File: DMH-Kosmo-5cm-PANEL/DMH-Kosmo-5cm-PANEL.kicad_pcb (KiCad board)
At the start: 2 copper layers, 50 x 200 mm, 4 parts

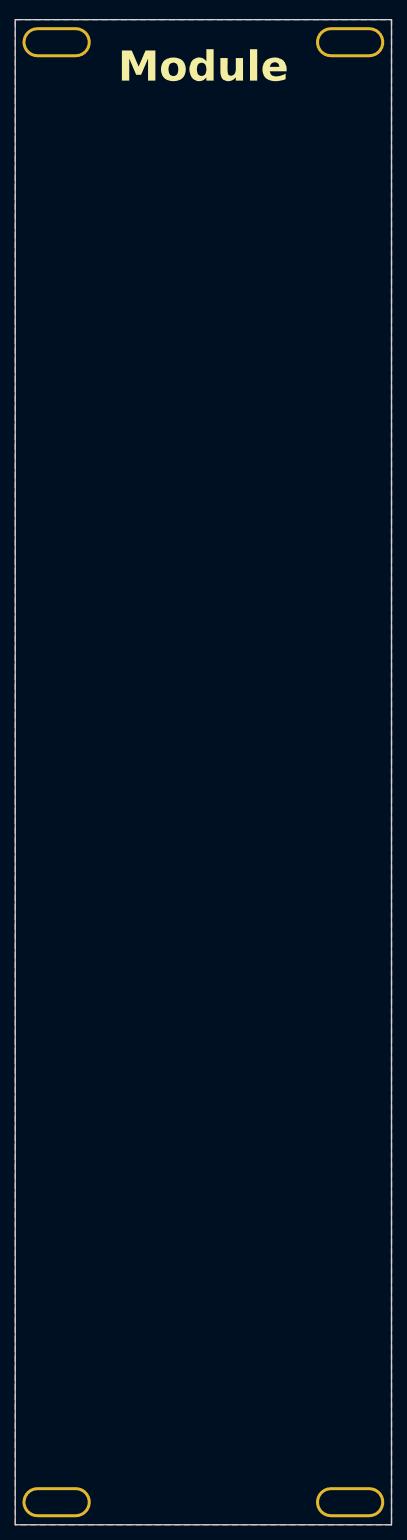
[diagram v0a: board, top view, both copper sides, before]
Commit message: Finished 5cm Panel template
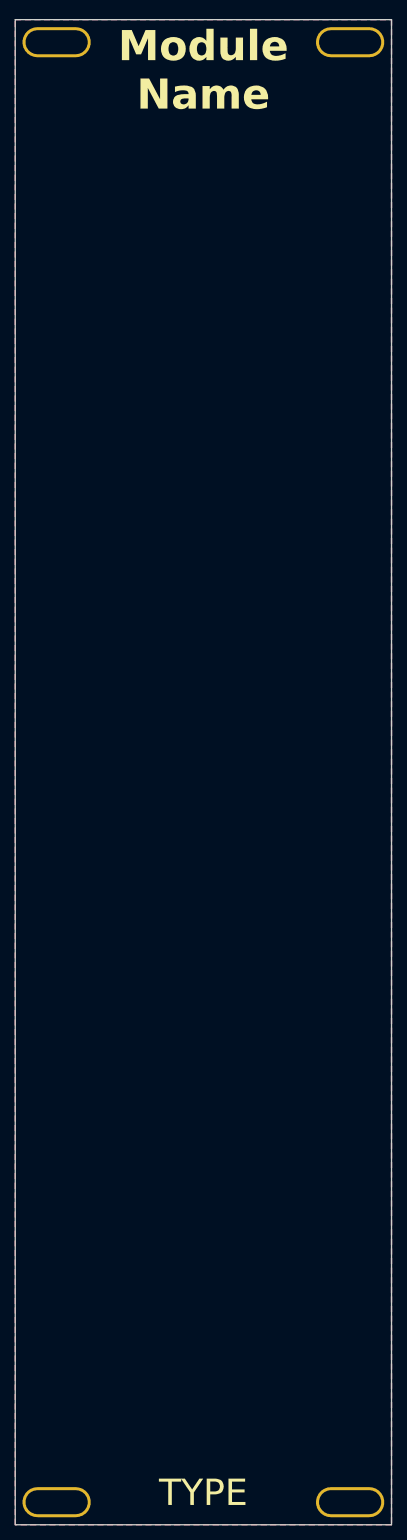
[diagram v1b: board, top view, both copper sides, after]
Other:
- board text added: "Module Name"
- board text added: "TYPE"
- board text removed: "Module"

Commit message: Updated 5cm and 10 templates
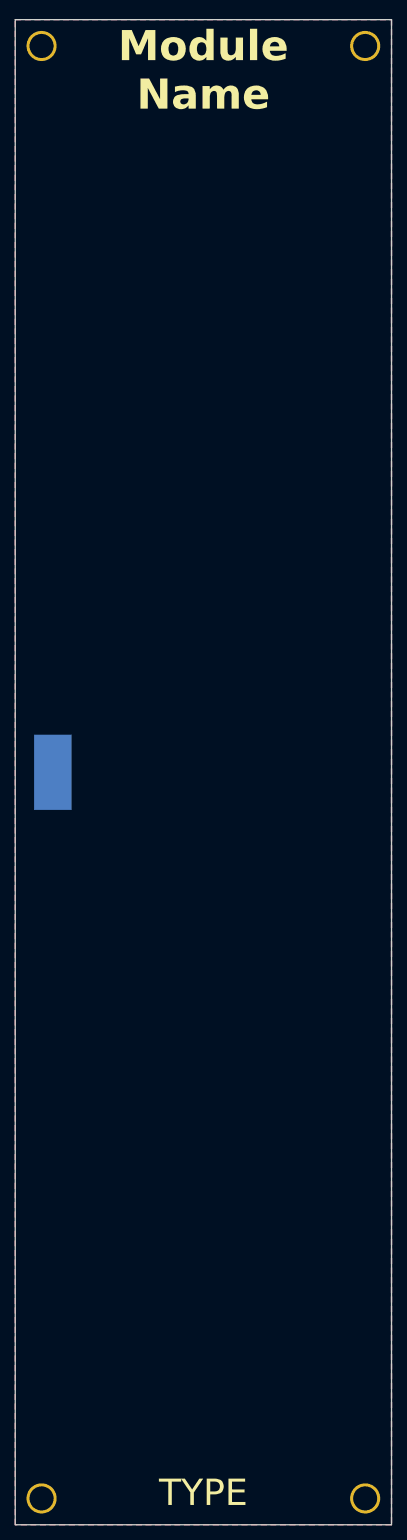
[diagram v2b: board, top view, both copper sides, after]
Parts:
- added J0: Panel_GND_Solder_Wire_Pad, SynthStuff:Panel_GND_SolderWirePad_5x10mm, B.Cu at (55.0, 130.0)
- H1, H2, H3, H4: footprint SynthStuff:MountingHole_Slotted_Rails -> SynthStuff:MountingHole_Rails
- moved H1 2.06 mm to (53.5, 33.5)
- moved H2 2.06 mm to (96.5, 33.5)
- moved H3 2.06 mm to (53.5, 226.5)
- moved H4 2.06 mm to (96.5, 226.5)
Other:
- board text added: "Mk1.0 - Month Year"
- board text removed: "JLCJLCJLCJLC"
